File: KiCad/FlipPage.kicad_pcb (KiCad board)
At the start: 2 copper layers, 59.7 x 62.2 mm, 5 parts, among them J1 Conn_01x02_Male, J2 Conn_01x02_Male, J3 USB_B_Mini, U1 Bluefruit_SPI_Bluetooth

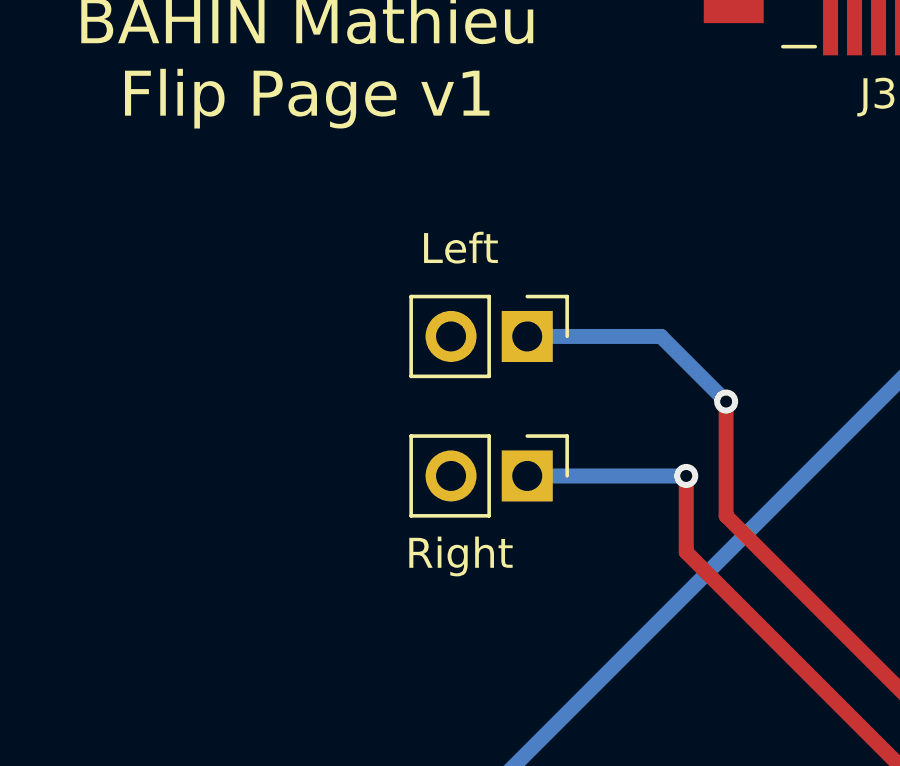
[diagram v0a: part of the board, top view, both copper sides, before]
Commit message: Added Front Silk Info for wiring
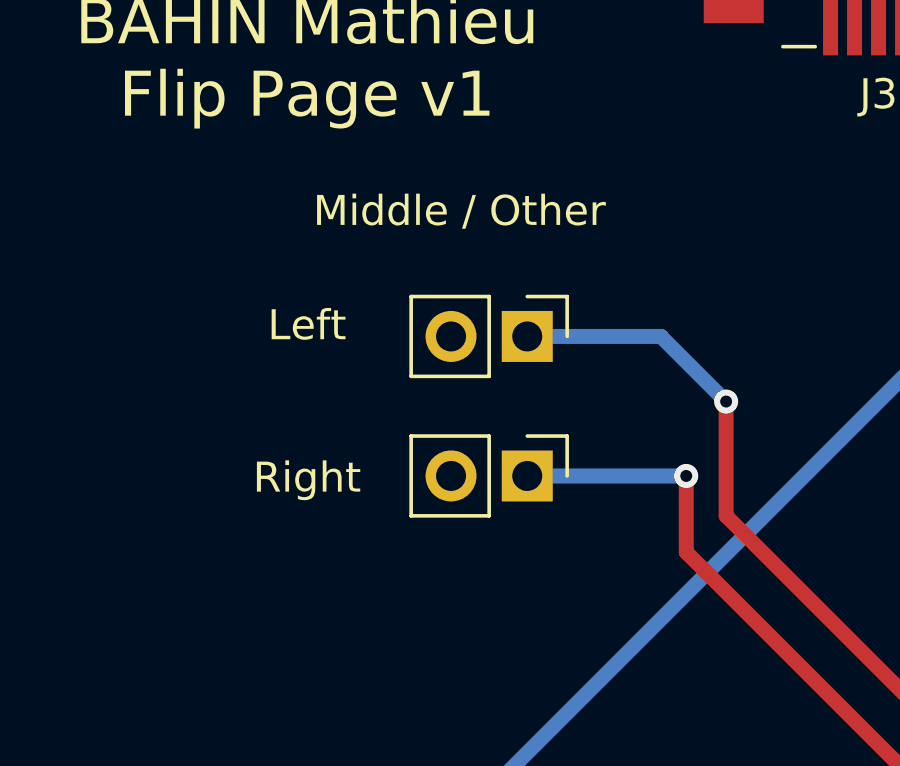
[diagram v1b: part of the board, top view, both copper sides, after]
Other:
- board text added: "Middle / Other"
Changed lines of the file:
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@@
   (general
     (thickness 1.6)
-    (drawings 13)
+    (drawings 14)
     (tracks 27)
     (zones 0)
@@
     (34 B.Paste user)
     (35 F.Paste user)
-    (36 B.SilkS user hide)
+    (36 B.SilkS user)
     (37 F.SilkS user)
     (38 B.Mask user hide)
@@
     (descr "Through hole straight pin header, 1x02, 2.54mm pitch, single row")
     (tags "Through hole pin header THT 1x02 2.54mm single row")
-    (fp_text reference J2 (at 0 7.34 180) (layer F.SilkS) hide
+    (fp_text reference J2 (at 1.33 -2.82 180) (layer F.SilkS) hide
       (effects (font (size 1 1) (thickness 0.15)))
     )
@@
     (descr "Through hole straight pin header, 1x02, 2.54mm pitch, single row")
     (tags "Through hole pin header THT 1x02 2.54mm single row")
-    (fp_text reference J1 (at -0.37 7.34 180) (layer F.SilkS) hide
+    (fp_text reference J1 (at 0.9 -2.82 180) (layer F.SilkS) hide
       (effects (font (size 1 1) (thickness 0.15)))
     )
@@
     )
   )
-  (gr_text Right (at 105.41 101.6) (layer F.SilkS)
+  (gr_text Right (at 100.33 99.06) (layer F.SilkS)
     (effects (font (size 1 1) (thickness 0.15)))
   )
-  (gr_text Left (at 105.41 91.44) (layer F.SilkS)
+  (gr_text Left (at 100.33 93.98) (layer F.SilkS)
     (effects (font (size 1 1) (thickness 0.15)))
   )
+  (gr_text "Middle / Other" (at 105.41 90.17) (layer F.SilkS)
+    (effects (font (size 1 1) (thickness 0.15)))
+  )

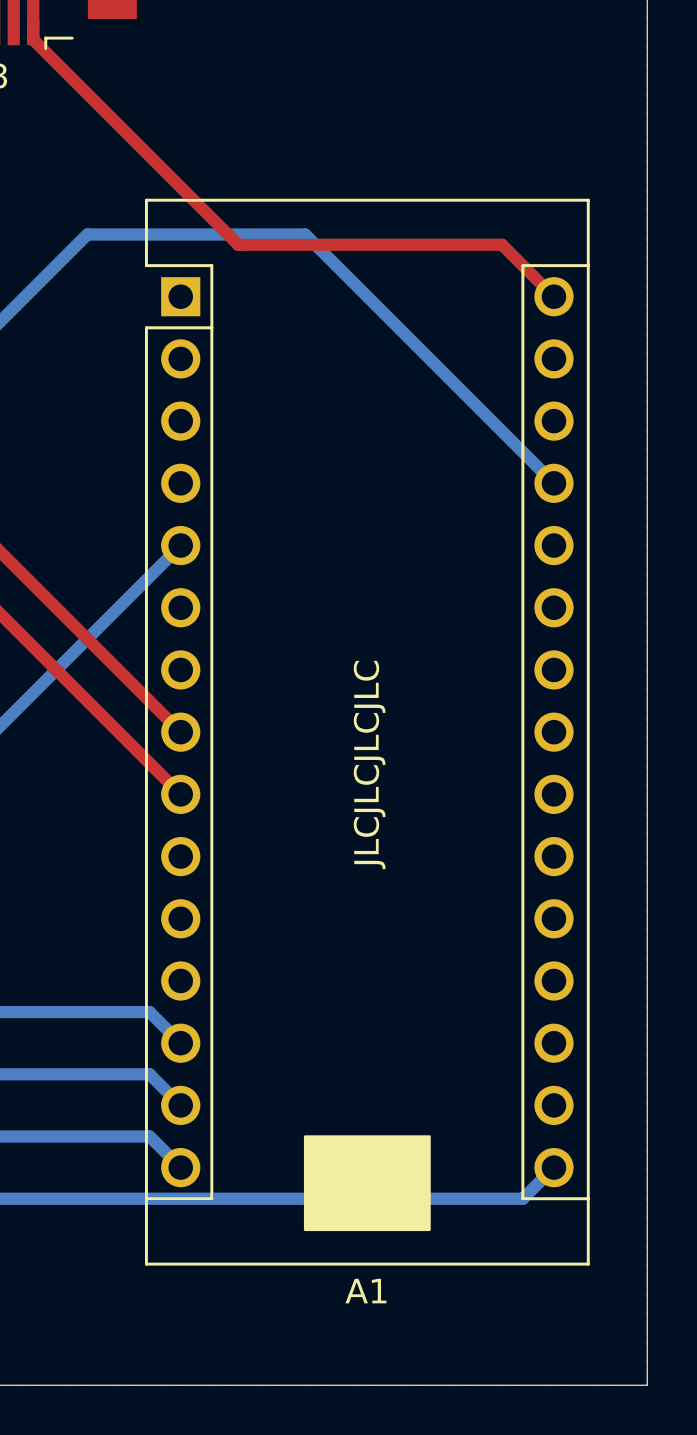
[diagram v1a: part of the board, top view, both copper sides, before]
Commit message: Modified links of libs
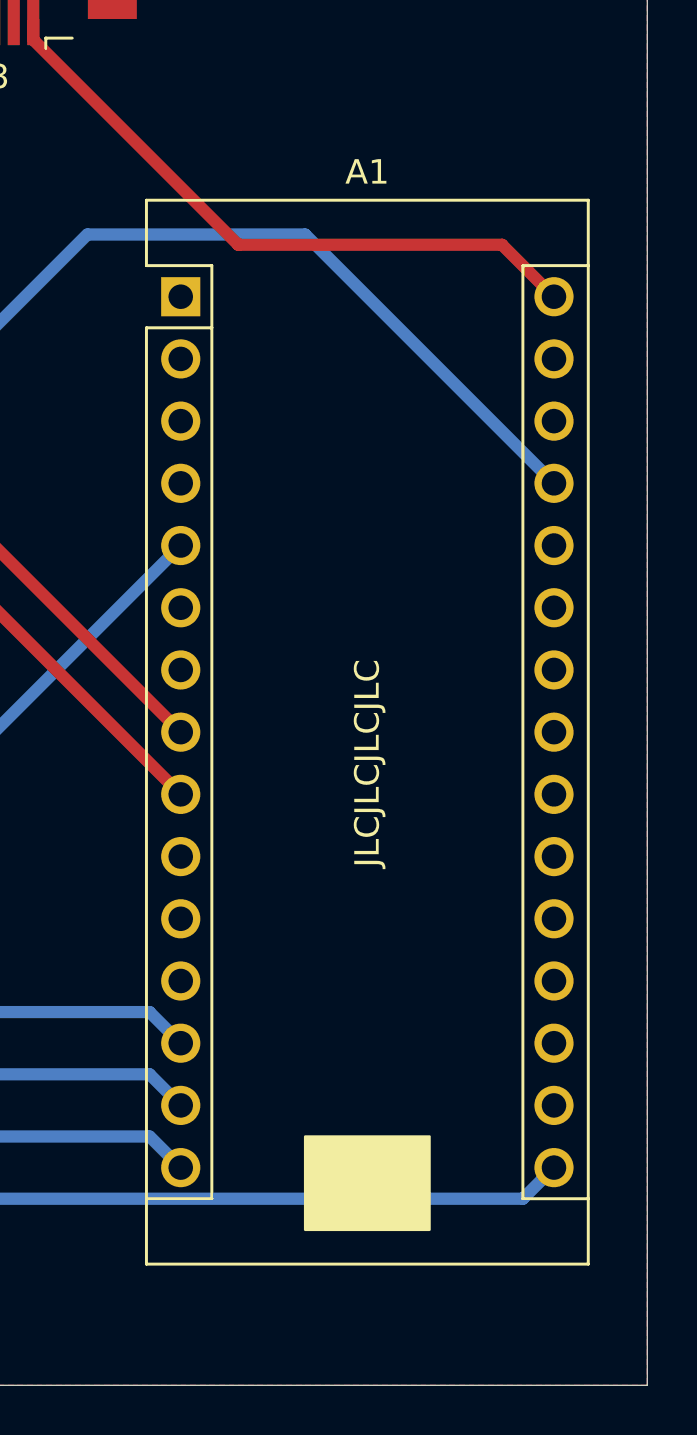
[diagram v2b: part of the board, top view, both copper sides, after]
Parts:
- A1: footprint librairie:Arduino_Nano_step -> perso:Arduino_Nano_step
- J3: footprint librairie:USB_Mini-B_Lumberg_2486_01_Horizontal -> perso:USB_Mini-B_Lumberg_2486_01_Horizontal
